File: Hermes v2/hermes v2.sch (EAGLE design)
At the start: 23 parts, among them Q1 NMOSFET, Q2 P-FET, Q3 NMOSFET, Q4 NMOSFET, Q5 P-FET, U1 DAC, U2 AD8067, X1 22-23-2051

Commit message: updated hermes
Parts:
- removed D2: (no value), zetex:DSOD323
- removed Q3, Q4: NMOSFET, N-FET:NMOSFET
- removed Q5: P-FET, P-FET:P-FET
- removed X1: 22-23-2051, con-molex:22-23-2051
- added AUTO: G, eagle-ltspice:LED_ESML0603
- added DZ1: LB10, led:LB10
- added IC1: LM3914V, national-semiconductor:LM3914V
- added K1: LCC110STR, relay:AQW654SMD
- added MAN: R, eagle-ltspice:LED_ESML0603
- added R10: 1.21k, resistor:R-US_R0603
- added R11, R8, R9: 10K, resistor:R-US_R0603
- added SV3: (no value), con-lstb:MA06-1
- D1: value (none) -> 3v3; device zetex:DSOD323 -> diode:ZENER; DIGI BAT54WS-FDICT-ND -> (none)
- Q1: value NMOSFET -> BSS123; device N-FET:NMOSFET -> transistor-small-signal:BSS123
- Q2: value P-FET -> BSS84; device P-FET:P-FET -> transistor-small-signal:BSS84; DIGI BSS84CT-ND -> (none)
- R1: value 15k -> 100
- R2: value 3k -> 2.03k
- R4: value 10k -> 20K
- R5: value 10k -> 15K
- R6, R7: value 10k -> 100
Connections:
- removed net ACC_POT_A: X1-3.S
- removed net ACC_POT_B: C2.1, U2.+VS, X1-5.S
- removed net DIGITAL_DRAIN: D1.A, Q2.DRAIN
- removed net DIGITAL_ENABLE: Q1.DRAIN, Q2.GATE, R4.2
- removed net INVERT_ENABLE: Q3.DRAIN, Q4.GATE, R5.2
- removed net MANUAL_DRAIN: D2.A, Q5.DRAIN
- removed net MANUAL_ENABLE: Q4.DRAIN, Q5.GATE, R6.2
- removed net THROTTLE_1: R1.1, X1-4.S
- removed net THROTTLE_2: D1.C, D2.C, X1-2.S
- new net CONTROL_+: K1-1.K, R1.1
- new net N$1: DZ1-10.C, IC1.LED1
- new net N$10: DZ1-5.C, IC1.LED6
- new net N$11: DZ1-4.C, IC1.LED7
- new net N$12: DZ1-3.C, IC1.LED8
- new net N$13: DZ1-2.C, IC1.LED9
- new net N$14: DZ1-1.C, IC1.LED10
- new net N$15: IC1.REFADJ, R10.2, R11.1
- new net N$16: IC1.REFOUT, IC1.RHI, R10.1
- new net N$2: AUTO.C, Q1.D
- new net N$3: MAN.A, R7.2
- new net N$4: AUTO.A, R6.2
- new net N$5: Q2.D, R7.1
- new net N$6: DZ1-9.C, IC1.LED2
- new net N$7: DZ1-8.C, IC1.LED3
- new net N$8: DZ1-7.C, IC1.LED4
- new net N$9: DZ1-6.C, IC1.LED5
- new net THROTTLE_+: SV3.2, SV3.5
- new net THROTTLE_S: IC1.SIGIN, K1-1.D1, K1-2.D1, SV3.1
- new net TH_ADC: D1.C, R4.2, R5.1, SV1.8
- net ACC_POT_W: now also K1-1.D2, R4.1, SV3.4; no longer Q5.SOURCE, R6.1, X1-1.S
- net ENABLE: now also Q1.G, Q2.G, R1.2, R8.1, R9.2; no longer Q1.GATE, Q3.GATE, R7.1
- net GND: now also D1.A, IC1.RLO, IC1.V-, K1-2.A, MAN.C, Q1.S, R11.2, R5.2, R8.2, SV3.3, SV3.6; no longer Q1.SOURCE, Q3.SOURCE, Q4.SOURCE, R1.2, R7.2
- net OP_AMP_OUT: now also K1-2.D2; no longer Q2.SOURCE, R4.1
- net PP12V: now also C2.1, IC1.MODE, IC1.V+, U2.+VS
- net PP3V3: now also DZ1-1.A, DZ1-10.A, DZ1-2.A, DZ1-3.A, DZ1-4.A, DZ1-5.A, DZ1-6.A, DZ1-7.A, DZ1-8.A, DZ1-9.A, Q2.S, R6.1, R9.1; no longer R5.1
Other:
- moved on the sheet: C1, C2, R1, R2, R3, R4, R5, R6, R7, U1, U2

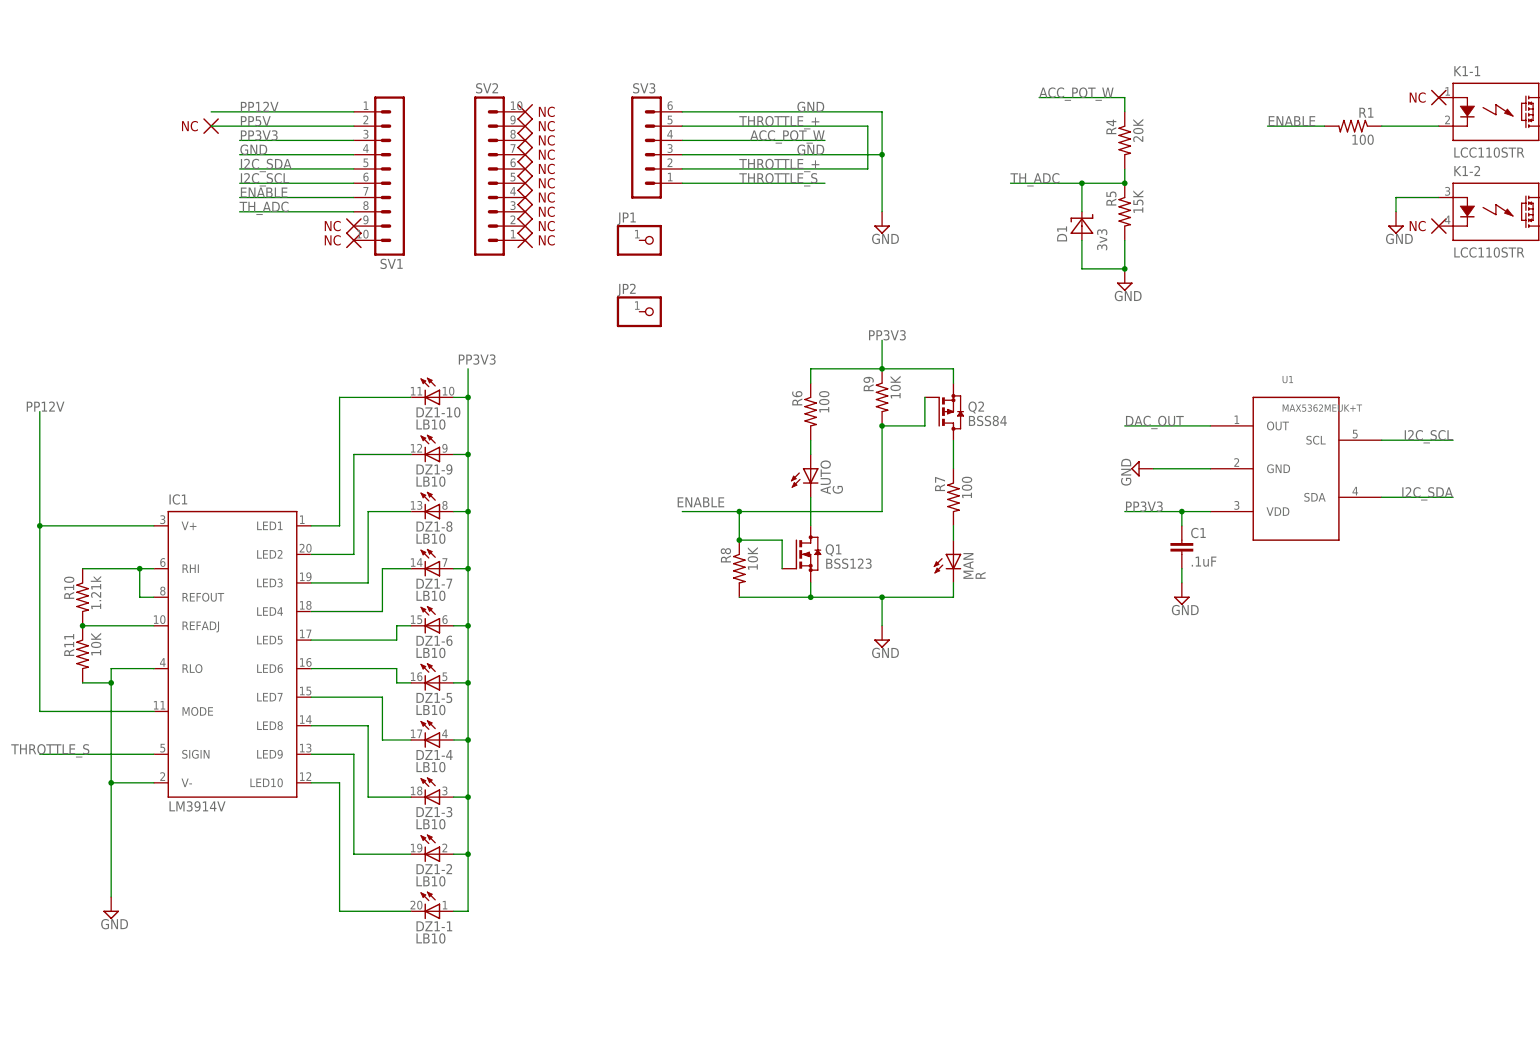
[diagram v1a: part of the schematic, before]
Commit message: fixed hermes issues
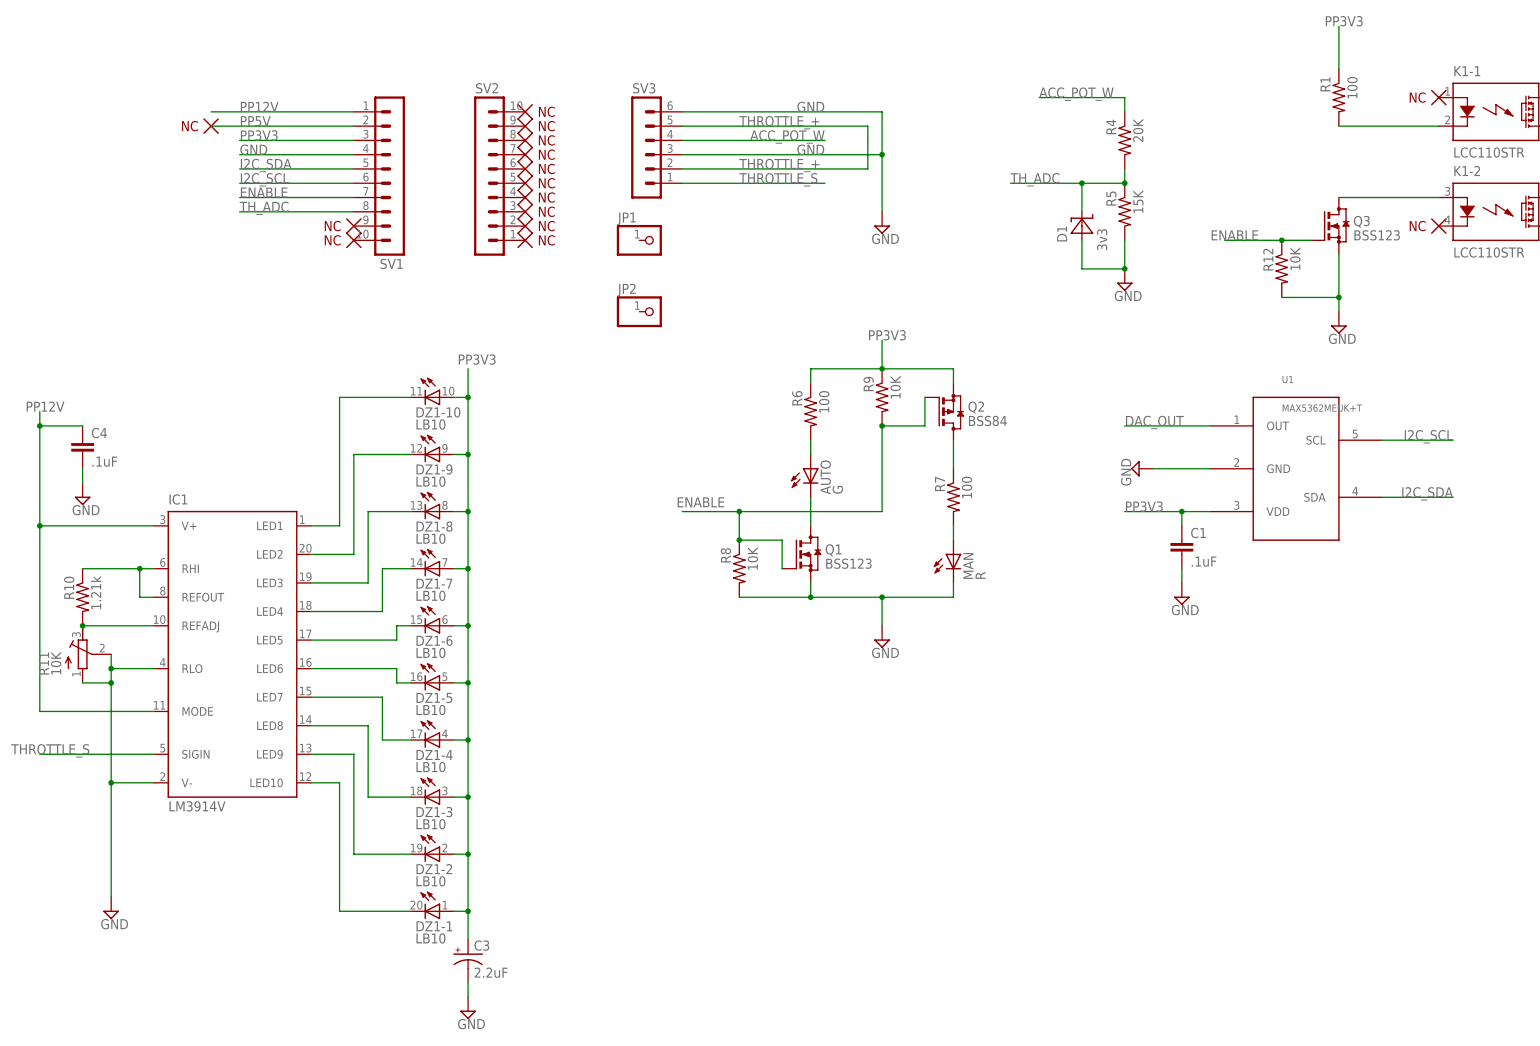
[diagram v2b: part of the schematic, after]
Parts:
- added C3: 2.2uF, rcl:CPOL-USSMCA
- added C4: .1uF, eagle-ltspice:CC0402
- added Q3: BSS123, transistor-small-signal:BSS123
- added R12: 10K, resistor:R-US_R0603
- R11: device resistor:R-US_R0603 -> rcl:R-TRIMM5X; DIGI (none) -> 490-2678-1-ND
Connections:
- new net CONTROL_-: K1-2.A, Q3.D
- net CONTROL_+: now also R1.2; no longer R1.1
- net ENABLE: now also Q3.G, R12.1; no longer R1.2
- net GND: now also C3.-, C4.2, Q3.S, R11.A, R11.S, R12.2; no longer K1-2.A, R11.2
- net N$15: now also R11.E; no longer R11.1
- net PP12V: now also C4.1
- net PP3V3: now also C3.+, R1.1
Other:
- moved on the sheet: R1
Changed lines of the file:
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@@
 <?xml version="1.0" encoding="utf-8"?>
 <!DOCTYPE eagle SYSTEM "eagle.dtd">
-<eagle version="7.6.0">
+<eagle version="7.7.0">
 <drawing>
 <settings>
@@
 <layer number="97" name="Info" color="7" fill="1" visible="yes" active="yes"/>
 <layer number="98" name="Guide" color="6" fill="1" visible="yes" active="yes"/>
-<layer number="99" name="SpiceOrder" color="5" fill="1" visible="yes" active="yes"/>
+<layer number="99" name="SpiceOrder" color="5" fill="1" visible="no" active="yes"/>
 </layers>
 <schematic xreflabel="%F%N/%S.%C%R" xrefpart="/%S.%C%R">
@@
 <part name="SUPPLY10" library="supply2" deviceset="GND" device=""/>
 <part name="R10" library="resistor" deviceset="R-US_" device="R0603" value="1.21k"/>
-<part name="R11" library="resistor" deviceset="R-US_" device="R0603" value="10K"/>
+<part name="Q3" library="transistor-small-signal" deviceset="BSS123" device=""/>
+<part name="R12" library="resistor" deviceset="R-US_" device="R0603" value="10K"/>
+<part name="C3" library="rcl" deviceset="CPOL-US" device="SMCA" value="2.2uF">
+<attribute name="DIGI" value="478-3119-2-ND"/>
+</part>
+<part name="SUPPLY11" library="supply2" deviceset="GND" device=""/>
+<part name="C4" library="eagle-ltspice" deviceset="C" device="C0402" value=".1uF"/>
+<part name="SUPPLY12" library="supply2" deviceset="GND" device=""/>
+<part name="R11" library="rcl" deviceset="R-TRIMM" device="5X" value="10K">
+<attribute name="DIGI" value="490-2678-1-ND"/>
+</part>
 </parts>
 <sheets>
@@
 <instance part="K1" gate="-1" x="198.12" y="116.84"/>
 <instance part="K1" gate="-2" x="198.12" y="99.06"/>
-<instance part="SUPPLY6" gate="GND" x="180.34" y="96.52"/>
+<instance part="SUPPLY6" gate="GND" x="170.18" y="78.74"/>
 <instance part="U$16" gate="G$1" x="187.96" y="119.38" rot="R180"/>
 <instance part="U$17" gate="G$1" x="187.96" y="96.52" rot="R180"/>
-<instance part="R1" gate="G$1" x="172.72" y="114.3" rot="MR0"/>
+<instance part="R1" gate="G$1" x="170.18" y="119.38" rot="MR270"/>
 <instance part="R4" gate="G$1" x="132.08" y="111.76" rot="MR270"/>
 <instance part="R5" gate="G$1" x="132.08" y="99.06" rot="MR270"/>
@@
 <instance part="SUPPLY10" gate="GND" x="-48.26" y="-25.4"/>
 <instance part="R10" gate="G$1" x="-53.34" y="30.48" rot="MR270"/>
-<instance part="R11" gate="G$1" x="-53.34" y="20.32" rot="MR270"/>
+<instance part="Q3" gate="G$1" x="170.18" y="96.52"/>
+<instance part="R12" gate="G$1" x="160.02" y="88.9" rot="MR270"/>
+<instance part="C3" gate="G$1" x="15.24" y="-33.02">
+<attribute name="DIGI" x="15.24" y="-33.02" size="1.778" layer="96" display="off"/>
+</instance>
+<instance part="SUPPLY11" gate="GND" x="15.24" y="-43.18"/>
+<instance part="C4" gate="G$1" x="-53.34" y="58.42"/>
+<instance part="SUPPLY12" gate="GND" x="-53.34" y="48.26"/>
+<instance part="R11" gate="G$1" x="-53.34" y="20.32">
+<attribute name="DIGI" x="-53.34" y="20.32" size="1.778" layer="96" display="off"/>
+</instance>
 </instances>
 <busses>
@@
 <wire x1="-60.96" y1="10.16" x2="-60.96" y2="43.18" width="0.1524" layer="91"/>
 <pinref part="IC1" gate="G$1" pin="V+"/>
-<wire x1="-60.96" y1="43.18" x2="-60.96" y2="63.5" width="0.1524" layer="91"/>
+<wire x1="-60.96" y1="43.18" x2="-60.96" y2="60.96" width="0.1524" layer="91"/>
+<wire x1="-60.96" y1="60.96" x2="-60.96" y2="63.5" width="0.1524" layer="91"/>
 <wire x1="-40.64" y1="43.18" x2="-60.96" y2="43.18" width="0.1524" layer="91"/>
 <junction x="-60.96" y="43.18"/>
 <label x="-63.5" y="63.5" size="1.778" layer="95"/>
+<pinref part="C4" gate="G$1" pin="1"/>
+<wire x1="-53.34" y1="60.96" x2="-60.96" y2="60.96" width="0.1524" layer="91"/>
+<junction x="-60.96" y="60.96"/>
 </segment>
 </net>
@@
 <label x="78.74" y="116.84" size="1.778" layer="95" rot="MR0"/>
 <pinref part="SV3" gate="1" pin="6"/>
-</segment>
-<segment>
-<pinref part="K1" gate="-2" pin="A"/>
-<wire x1="187.96" y1="101.6" x2="180.34" y2="101.6" width="0.1524" layer="91"/>
-<wire x1="180.34" y1="101.6" x2="180.34" y2="99.06" width="0.1524" layer="91"/>
-<pinref part="SUPPLY6" gate="GND" pin="GND"/>
 </segment>
 <segment>
@@
 <pinref part="SUPPLY10" gate="GND" pin="GND"/>
 <wire x1="-48.26" y1="-2.54" x2="-48.26" y2="-22.86" width="0.1524" layer="91"/>
-<pinref part="R11" gate="G$1" pin="2"/>
 <wire x1="-53.34" y1="15.24" x2="-48.26" y2="15.24" width="0.1524" layer="91"/>
 <junction x="-48.26" y="15.24"/>
+<wire x1="-48.26" y1="20.32" x2="-48.26" y2="17.78" width="0.1524" layer="91"/>
+<junction x="-48.26" y="17.78"/>
+<pinref part="R11" gate="G$1" pin="A"/>
+<pinref part="R11" gate="G$1" pin="S"/>
+</segment>
+<segment>
+<pinref part="Q3" gate="G$1" pin="S"/>
+<pinref part="SUPPLY6" gate="GND" pin="GND"/>
+<wire x1="170.18" y1="91.44" x2="170.18" y2="83.82" width="0.1524" layer="91"/>
+<pinref part="R12" gate="G$1" pin="2"/>
+<wire x1="170.18" y1="83.82" x2="170.18" y2="81.28" width="0.1524" layer="91"/>
+<wire x1="160.02" y1="83.82" x2="170.18" y2="83.82" width="0.1524" layer="91"/>
+<junction x="170.18" y="83.82"/>
+</segment>
+<segment>
+<pinref part="C3" gate="G$1" pin="-"/>
+<pinref part="SUPPLY11" gate="GND" pin="GND"/>
+<wire x1="15.24" y1="-40.64" x2="15.24" y2="-38.1" width="0.1524" layer="91"/>
+</segment>
+<segment>
+<pinref part="C4" gate="G$1" pin="2"/>
+<pinref part="SUPPLY12" gate="GND" pin="GND"/>
+<wire x1="-53.34" y1="53.34" x2="-53.34" y2="50.8" width="0.1524" layer="91"/>
 </segment>
 </net>
@@
 <label x="-25.4" y="101.6" size="1.778" layer="95"/>
 <pinref part="SV1" gate="1" pin="7"/>
-</segment>
-<segment>
-<pinref part="R1" gate="G$1" pin="2"/>
-<wire x1="167.64" y1="114.3" x2="157.48" y2="114.3" width="0.1524" layer="91"/>
-<label x="157.48" y="114.3" size="1.778" layer="95"/>
 </segment>
 <segment>
@@
 <wire x1="63.5" y1="45.72" x2="53.34" y2="45.72" width="0.1524" layer="91"/>
 <junction x="63.5" y="45.72"/>
+</segment>
+<segment>
+<pinref part="Q3" gate="G$1" pin="G"/>
+<wire x1="165.1" y1="93.98" x2="160.02" y2="93.98" width="0.1524" layer="91"/>
+<pinref part="R12" gate="G$1" pin="1"/>
+<wire x1="160.02" y1="93.98" x2="149.86" y2="93.98" width="0.1524" layer="91"/>
+<junction x="160.02" y="93.98"/>
+<label x="147.32" y="93.98" size="1.778" layer="95"/>
 </segment>
 </net>
@@
 <junction x="15.24" y="35.56"/>
 <label x="20.32" y="73.66" size="1.778" layer="95" rot="R180"/>
+<pinref part="C3" gate="G$1" pin="+"/>
+<wire x1="15.24" y1="-30.48" x2="15.24" y2="-25.4" width="0.1524" layer="91"/>
+<junction x="15.24" y="-25.4"/>
+</segment>
+<segment>
+<pinref part="R1" gate="G$1" pin="1"/>
+<wire x1="170.18" y1="124.46" x2="170.18" y2="132.08" width="0.1524" layer="91"/>
+<label x="167.64" y="132.08" size="1.778" layer="95"/>
 </segment>
 </net>
@@
 <wire x1="-40.64" y1="2.54" x2="-60.96" y2="2.54" width="0.1524" layer="91"/>
 <label x="-66.04" y="2.54" size="1.778" layer="95"/>
-</segment>
-</net>
-<net name="CONTROL_+" class="0">
-<segment>
-<pinref part="R1" gate="G$1" pin="1"/>
-<pinref part="K1" gate="-1" pin="K"/>
-<wire x1="177.8" y1="114.3" x2="187.96" y2="114.3" width="0.1524" layer="91"/>
 </segment>
 </net>
@@
 <segment>
 <pinref part="R10" gate="G$1" pin="2"/>
-<pinref part="R11" gate="G$1" pin="1"/>
 <pinref part="IC1" gate="G$1" pin="REFADJ"/>
 <wire x1="-40.64" y1="25.4" x2="-53.34" y2="25.4" width="0.1524" layer="91"/>
+<pinref part="R11" gate="G$1" pin="E"/>
 <junction x="-53.34" y="25.4"/>
 </segment>
@@
 </segment>
 </net>
+<net name="CONTROL_+" class="0">
+<segment>
+<pinref part="K1" gate="-1" pin="K"/>
+<pinref part="R1" gate="G$1" pin="2"/>
+<wire x1="187.96" y1="114.3" x2="170.18" y2="114.3" width="0.1524" layer="91"/>
+</segment>
+</net>
+<net name="CONTROL_-" class="0">
+<segment>
+<pinref part="K1" gate="-2" pin="A"/>
+<pinref part="Q3" gate="G$1" pin="D"/>
+<wire x1="187.96" y1="101.6" x2="170.18" y2="101.6" width="0.1524" layer="91"/>
+</segment>
+</net>

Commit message: fixed more hermes things
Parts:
- removed SV3: (no value), con-lstb:MA06-1
- added R13: 0, rcl:R-US_R0402
- added X1: (no value), con-molex:22-23-2061
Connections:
- removed net THROTTLE_+: SV3.2, SV3.5
- new net THROTTLE_+M: R13.1, X1-5.S
- new net THROTTLE_+P: R13.2, X1-2.S
- net ACC_POT_W: now also X1-3.S; no longer SV3.4
- net GND: now also X1-1.S, X1-4.S; no longer SV3.3, SV3.6
- net THROTTLE_S: now also X1-6.S; no longer SV3.1
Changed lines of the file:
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@@
 <part name="JP2" library="pinhead" deviceset="PINHD-1X1" device=""/>
 <part name="SUPPLY9" library="supply2" deviceset="GND" device=""/>
-<part name="SV3" library="con-lstb" deviceset="MA06-1" device=""/>
 <part name="K1" library="relay" deviceset="AQW*" device="SMD" technology="654" value="LCC110STR"/>
 <part name="SUPPLY6" library="supply2" deviceset="GND" device=""/>
@@
 <attribute name="DIGI" value="490-2678-1-ND"/>
 </part>
+<part name="X1" library="con-molex" deviceset="22-23-2061" device=""/>
+<part name="R13" library="rcl" deviceset="R-US_" device="R0402" value="0"/>
+<part name="SUPPLY13" library="supply2" deviceset="GND" device=""/>
 </parts>
 <sheets>
@@
 <instance part="JP1" gate="G$1" x="48.26" y="93.98"/>
 <instance part="JP2" gate="G$1" x="48.26" y="81.28"/>
-<instance part="SUPPLY9" gate="GND" x="88.9" y="96.52"/>
-<instance part="SV3" gate="1" x="45.72" y="111.76"/>
+<instance part="SUPPLY9" gate="GND" x="91.44" y="96.52"/>
 <instance part="K1" gate="-1" x="198.12" y="116.84"/>
 <instance part="K1" gate="-2" x="198.12" y="99.06"/>
@@
 <attribute name="DIGI" x="-53.34" y="20.32" size="1.778" layer="96" display="off"/>
 </instance>
+<instance part="X1" gate="-1" x="50.8" y="116.84" rot="R180"/>
+<instance part="X1" gate="-2" x="50.8" y="114.3" rot="R180"/>
+<instance part="X1" gate="-3" x="50.8" y="111.76" rot="R180"/>
+<instance part="X1" gate="-4" x="50.8" y="109.22" rot="R180"/>
+<instance part="X1" gate="-5" x="50.8" y="106.68" rot="R180"/>
+<instance part="X1" gate="-6" x="50.8" y="104.14" rot="R180"/>
+<instance part="R13" gate="G$1" x="96.52" y="109.22" rot="R90"/>
+<instance part="SUPPLY13" gate="GND" x="104.14" y="96.52"/>
 </instances>
 <busses>
@@
 </segment>
 <segment>
-<wire x1="88.9" y1="116.84" x2="88.9" y2="109.22" width="0.1524" layer="91"/>
 <pinref part="SUPPLY9" gate="GND" pin="GND"/>
-<wire x1="88.9" y1="109.22" x2="88.9" y2="99.06" width="0.1524" layer="91"/>
-<wire x1="53.34" y1="109.22" x2="88.9" y2="109.22" width="0.1524" layer="91"/>
+<wire x1="91.44" y1="109.22" x2="91.44" y2="99.06" width="0.1524" layer="91"/>
+<wire x1="53.34" y1="109.22" x2="91.44" y2="109.22" width="0.1524" layer="91"/>
 <label x="78.74" y="109.22" size="1.778" layer="95" rot="MR0"/>
-<pinref part="SV3" gate="1" pin="3"/>
-<junction x="88.9" y="109.22"/>
-<wire x1="53.34" y1="116.84" x2="88.9" y2="116.84" width="0.1524" layer="91"/>
-<label x="78.74" y="116.84" size="1.778" layer="95" rot="MR0"/>
-<pinref part="SV3" gate="1" pin="6"/>
+<pinref part="X1" gate="-4" pin="S"/>
 </segment>
 <segment>
@@
 <pinref part="SUPPLY12" gate="GND" pin="GND"/>
 <wire x1="-53.34" y1="53.34" x2="-53.34" y2="50.8" width="0.1524" layer="91"/>
+</segment>
+<segment>
+<wire x1="53.34" y1="116.84" x2="104.14" y2="116.84" width="0.1524" layer="91"/>
+<pinref part="X1" gate="-1" pin="S"/>
+<label x="78.74" y="116.84" size="1.778" layer="95" rot="MR0"/>
+<pinref part="SUPPLY13" gate="GND" pin="GND"/>
+<wire x1="104.14" y1="116.84" x2="104.14" y2="99.06" width="0.1524" layer="91"/>
 </segment>
 </net>
@@
 <wire x1="53.34" y1="111.76" x2="78.74" y2="111.76" width="0.1524" layer="91"/>
 <label x="78.74" y="111.76" size="1.778" layer="95" rot="MR0"/>
-<pinref part="SV3" gate="1" pin="4"/>
+<pinref part="X1" gate="-3" pin="S"/>
 </segment>
 <segment>
@@
 </segment>
 </net>
-<net name="THROTTLE_+" class="0">
-<segment>
-<pinref part="SV3" gate="1" pin="5"/>
-<wire x1="53.34" y1="114.3" x2="86.36" y2="114.3" width="0.1524" layer="91"/>
+<net name="THROTTLE_+P" class="0">
+<segment>
+<wire x1="53.34" y1="114.3" x2="96.52" y2="114.3" width="0.1524" layer="91"/>
 <label x="63.5" y="114.3" size="1.778" layer="95"/>
-<wire x1="86.36" y1="114.3" x2="86.36" y2="106.68" width="0.1524" layer="91"/>
-<pinref part="SV3" gate="1" pin="2"/>
-<wire x1="53.34" y1="106.68" x2="86.36" y2="106.68" width="0.1524" layer="91"/>
-<label x="63.5" y="106.68" size="1.778" layer="95"/>
+<pinref part="X1" gate="-2" pin="S"/>
+<pinref part="R13" gate="G$1" pin="2"/>
 </segment>
 </net>
@@
 <wire x1="53.34" y1="104.14" x2="78.74" y2="104.14" width="0.1524" layer="91"/>
 <label x="63.5" y="104.14" size="1.778" layer="95"/>
-<pinref part="SV3" gate="1" pin="1"/>
+<pinref part="X1" gate="-6" pin="S"/>
 </segment>
 <segment>
@@
 </segment>
 </net>
+<net name="THROTTLE_+M" class="0">
+<segment>
+<wire x1="53.34" y1="106.68" x2="88.9" y2="106.68" width="0.1524" layer="91"/>
+<pinref part="X1" gate="-5" pin="S"/>
+<label x="63.5" y="106.68" size="1.778" layer="95"/>
+<wire x1="88.9" y1="106.68" x2="88.9" y2="104.14" width="0.1524" layer="91"/>
+<pinref part="R13" gate="G$1" pin="1"/>
+<wire x1="88.9" y1="104.14" x2="96.52" y2="104.14" width="0.1524" layer="91"/>
+</segment>
+</net>
